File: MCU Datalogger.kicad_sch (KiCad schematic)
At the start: 25 parts, among them U1 24LC1025, U2 DS1337S_, U3 24LC1025, U4 ATMEGA328P-AU, Y1 32.768 KHz, Y2 16 MHz

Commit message: Completed Schematics and worked on comments
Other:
- note added: "ATMEGA MCU"
- note added: "EEPROM"
- note added: "Mounting Holes"
- note added: "Real Time Clock"
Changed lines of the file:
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@@
+		)
+	)
+	(rectangle
+		(start 29.21 129.54)
+		(end 133.35 175.26)
+		(stroke
+			(width 0)
+			(type default)
+		)
+		(fill
+			(type none)
+		)
+	)
+	(rectangle
+		(start 224.79 120.65)
+		(end 251.46 154.94)
+		(stroke
+			(width 0)
+			(type default)
+		)
+		(fill
+			(type none)
+		)
+	)
+	(rectangle
+		(start 140.97 22.86)
+		(end 266.7 110.49)
+		(stroke
+			(width 0)
+			(type default)
+		)
+		(fill
+			(type none)
+		)
+	)
+	(rectangle
+		(start 36.83 38.1)
+		(end 130.81 86.36)
+		(stroke
+			(width 0)
+			(type default)
+		)
+		(fill
+			(type none)
+		)
+	)
+	(text "Mounting Holes"
+		(exclude_from_sim no)
+		(at 232.41 119.38 0)
+		(effects
+			(font
+				(size 1.27 1.27)
+			)
+		)
+	)
+	(text "EEPROM"
+		(exclude_from_sim no)
+		(at 33.02 128.27 0)
+		(effects
+			(font
+				(size 1.27 1.27)
+			)
+		)
+	)
+	(text "ATMEGA MCU"
+		(exclude_from_sim no)
+		(at 147.32 20.32 0)
+		(effects
+			(font
+				(size 1.27 1.27)
+			)
+		)
+	)
+	(text "Real Time Clock"
+		(exclude_from_sim no)
+		(at 44.45 36.83 0)
+		(effects
+			(font
+				(size 1.27 1.27)
+			)
 		)
 	)

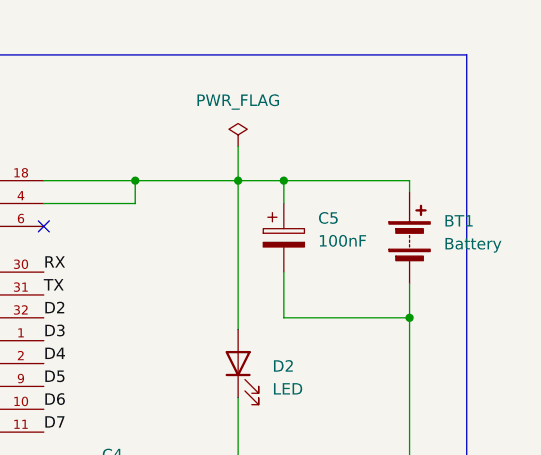
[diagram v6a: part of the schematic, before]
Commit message: Finished routing, silkscreen setup of the 2layer pcb
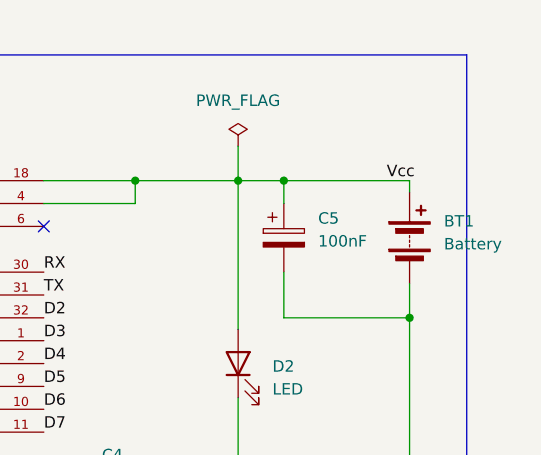
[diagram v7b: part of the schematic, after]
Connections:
- net Vcc: now also BT1.1 (+), C5.1, D2.2 (A), U4.18 (AVCC), U4.4 (VCC)
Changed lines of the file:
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@@
+		)
+	)
+	(label "Vcc"
+		(at 257.81 36.83 0)
+		(fields_autoplaced yes)
+		(effects
+			(font
+				(size 1.27 1.27)
+			)
+			(justify left bottom)
 		)
 	)

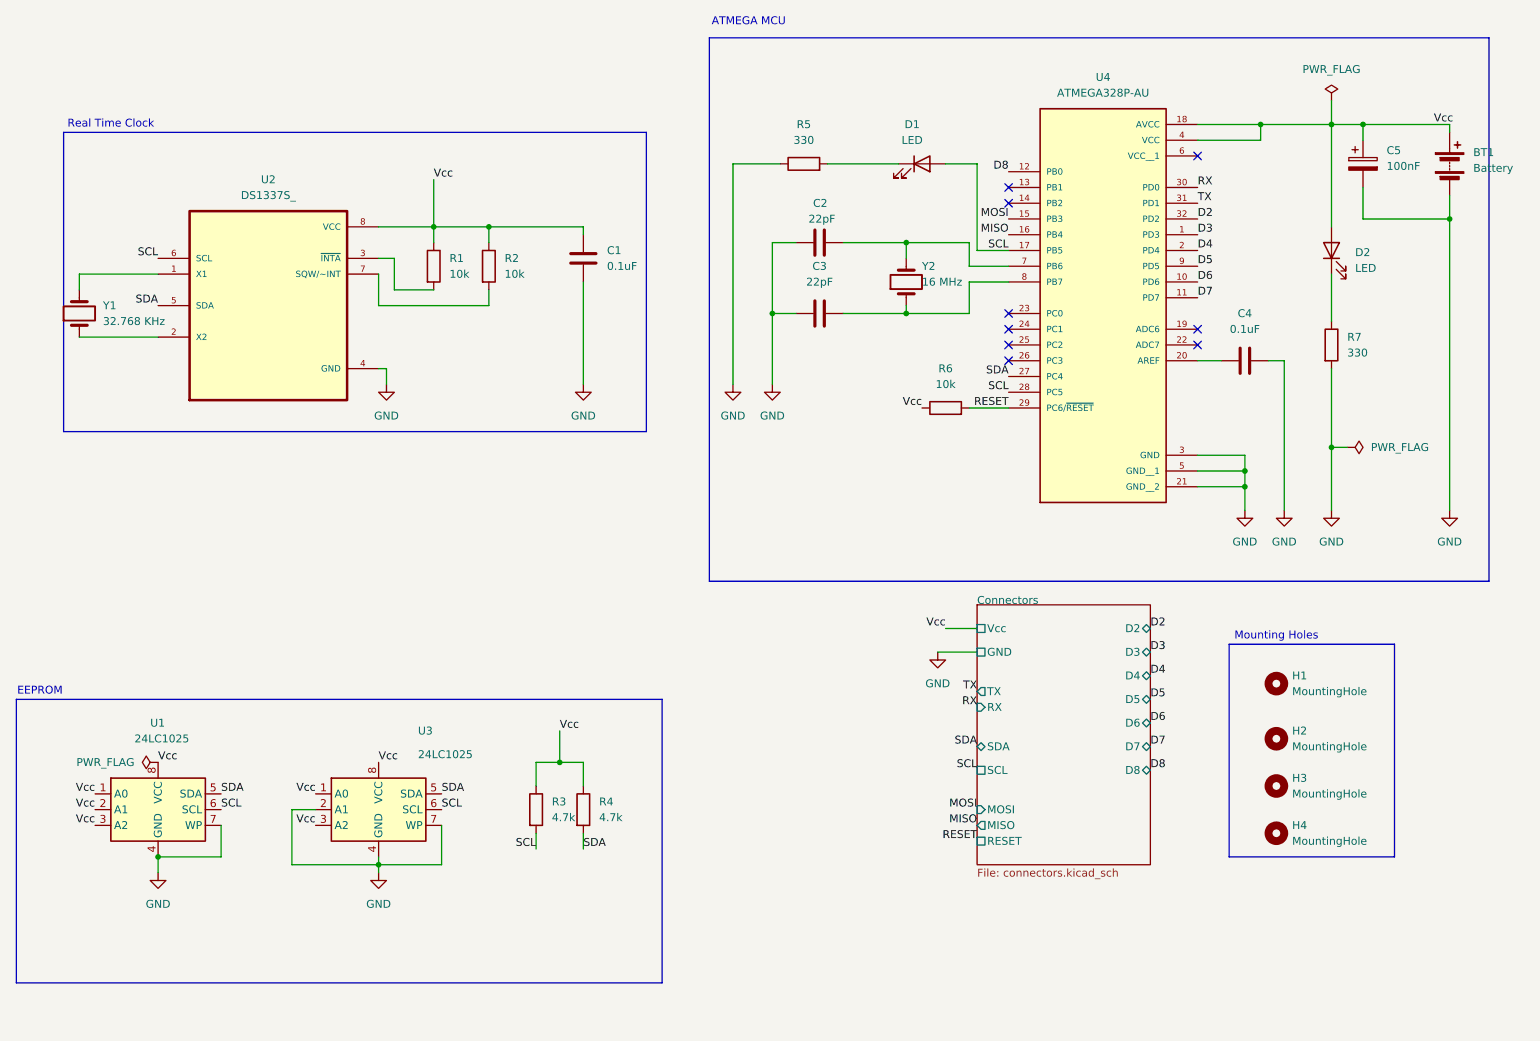
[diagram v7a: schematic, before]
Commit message: Fixed errors in the schematic
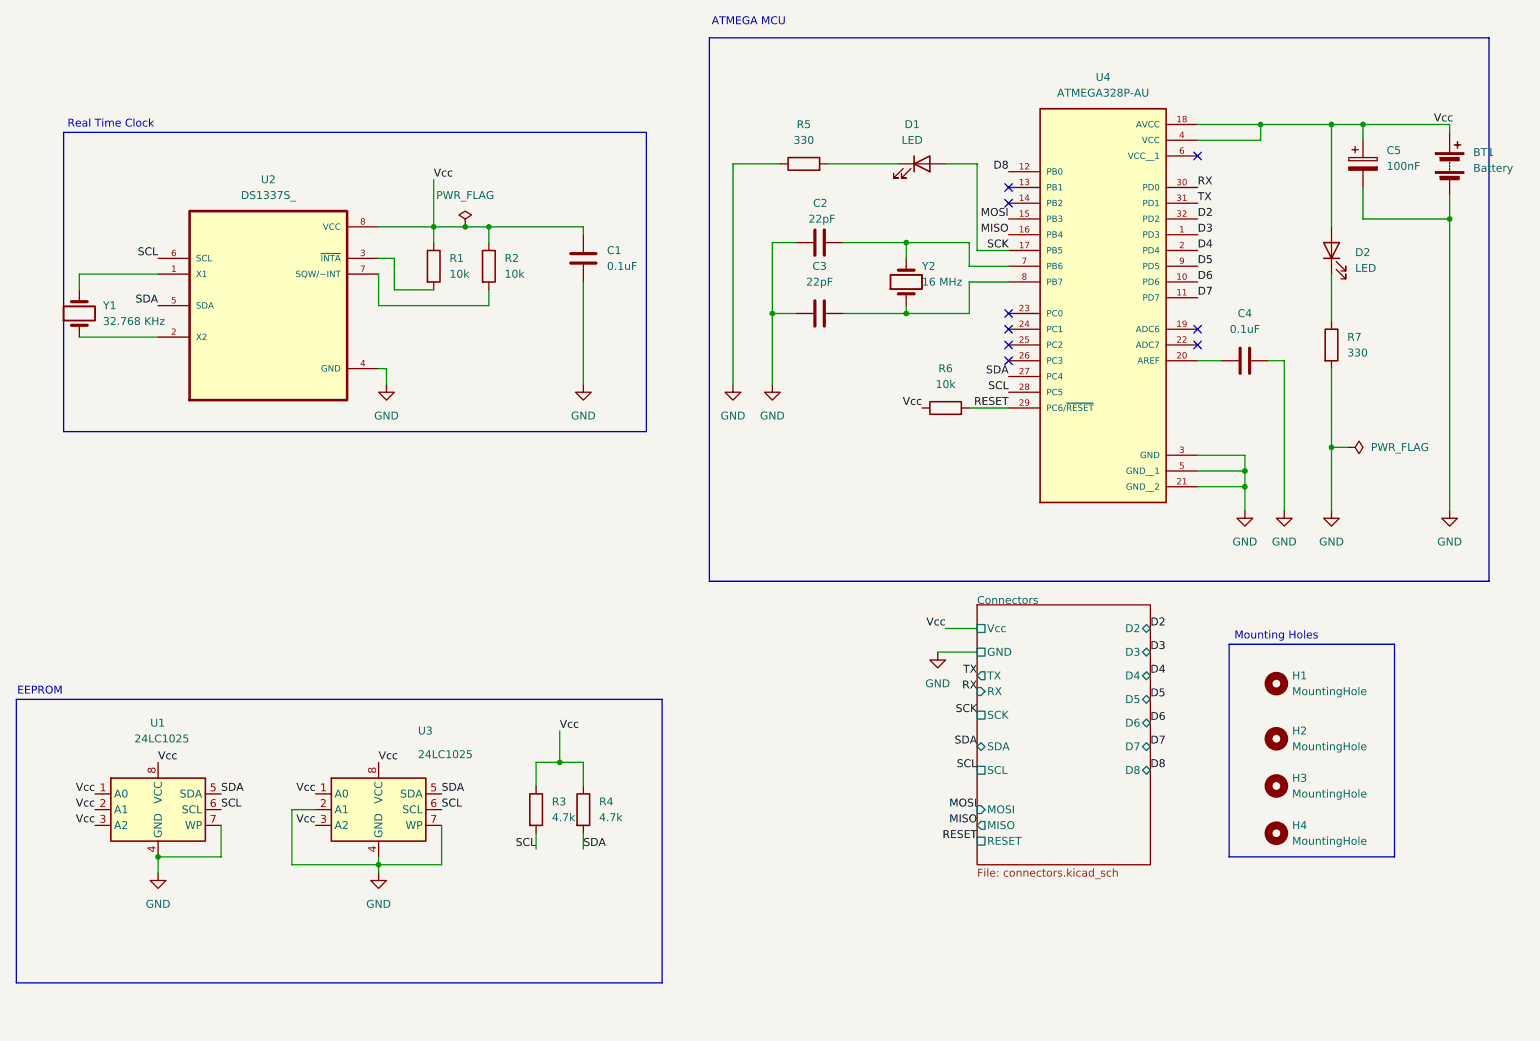
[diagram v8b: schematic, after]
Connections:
- net SCL: no longer D1.2 (A), U4.17 (PB5)
- new net SCK: D1.2 (A), U4.17 (PB5)
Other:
- sheet Connectors ports: added SCK; removed none
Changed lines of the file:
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@@
 	)
 	(junction
+		(at 101.6 53.34)
+		(diameter 0)
+		(color 0 0 0 0)
+	)
+	(junction
 		(at 229.87 36.83)
 		(diameter 0)
@@
 	(wire
 		(pts
-			(xy 241.3 33.02) (xy 241.3 36.83)
-		)
-		(stroke
-			(width 0)
-			(type default)
-		)
-	)
-	(wire
-		(pts
 			(xy 62.23 154.94) (xy 52.07 154.94)
 		)
@@
 	(wire
 		(pts
+			(xy 101.6 53.34) (xy 105.41 53.34)
+		)
+		(stroke
+			(width 0)
+			(type default)
+		)
+	)
+	(wire
+		(pts
 			(xy 77.47 147.32) (xy 73.66 147.32)
 		)
@@
 	(wire
 		(pts
+			(xy 105.41 53.34) (xy 120.65 53.34)
+		)
+		(stroke
+			(width 0)
+			(type default)
+		)
+	)
+	(wire
+		(pts
 			(xy 241.3 76.2) (xy 241.3 88.9)
 		)
@@
 	(wire
 		(pts
-			(xy 96.52 53.34) (xy 105.41 53.34)
+			(xy 96.52 53.34) (xy 101.6 53.34)
 		)
 		(stroke
@@
 	(wire
 		(pts
-			(xy 105.41 53.34) (xy 120.65 53.34)
-		)
-		(stroke
-			(width 0)
-			(type default)
-		)
-	)
-	(wire
-		(pts
 			(xy 229.87 39.37) (xy 229.87 36.83)
 		)
@@
 		)
 	)
-	(label "SCL"
+	(label "SCK"
 		(at 189.23 57.15 180)
 		(fields_autoplaced yes)
@@
 		)
 	)
+	(label "SCK"
+		(at 184.15 132.08 180)
+		(fields_autoplaced yes)
+		(effects
+			(font
+				(size 1.27 1.27)
+			)
+			(justify right bottom)
+		)
+	)
 	(label "TX"
 		(at 219.71 49.53 0)
@@
 	)
 	(label "RX"
-		(at 184.15 130.81 180)
+		(at 184.15 128.27 180)
 		(fields_autoplaced yes)
 		(effects
@@
 	)
 	(label "TX"
-		(at 184.15 128.27 180)
+		(at 184.15 125.73 180)
 		(fields_autoplaced yes)
 		(effects
@@
 	)
 	(symbol
-		(lib_id "power:PWR_FLAG")
-		(at 52.07 139.7 90)
-		(unit 1)
-		(exclude_from_sim no)
-		(in_bom yes)
-		(on_board yes)
-		(dnp no)
-		(fields_autoplaced yes)
-		(property "Reference" "#FLG03"
-			(at 50.165 139.7 0)
-			(effects
-				(font
-					(size 1.27 1.27)
-				)
-				(hide yes)
-			)
-		)
-		(property "Value" "PWR_FLAG"
-			(at 48.26 139.6999 90)
-			(effects
-				(font
-					(size 1.27 1.27)
-				)
-				(justify left)
-			)
-		)
-		(property "Footprint" ""
-			(at 52.07 139.7 0)
-			(effects
-				(font
-					(size 1.27 1.27)
-				)
-				(hide yes)
-			)
-		)
-		(property "Datasheet" "~"
-			(at 52.07 139.7 0)
-			(effects
-				(font
-					(size 1.27 1.27)
-				)
-				(hide yes)
-			)
-		)
-		(property "Description" "Special symbol for telling ERC where power comes from"
-			(at 52.07 139.7 0)
-			(effects
-				(font
-					(size 1.27 1.27)
-				)
-				(hide yes)
-			)
-		)
-		(pin "1"
-		)
-		(instances
-			(project "MCU Datalogger"
-				(path "/f5eacbf3-5133-41a8-b529-b36a541e7d42"
-					(reference "#FLG03")
-					(unit 1)
-				)
-			)
-		)
-	)
-	(symbol
 		(lib_id "Mechanical:MountingHole")
 		(at 232.41 151.13 0)
@@
 	)
 	(symbol
-		(lib_id "power:PWR_FLAG")
-		(at 241.3 33.02 0)
-		(unit 1)
-		(exclude_from_sim no)
-		(in_bom yes)
-		(on_board yes)
-		(dnp no)
-		(fields_autoplaced yes)
-		(property "Reference" "#FLG01"
-			(at 241.3 31.115 0)
-			(effects
-				(font
-					(size 1.27 1.27)
-				)
-				(hide yes)
-			)
-		)
-		(property "Value" "PWR_FLAG"
-			(at 241.3 27.94 0)
-			(effects
-				(font
-					(size 1.27 1.27)
-				)
-			)
-		)
-		(property "Footprint" ""
-			(at 241.3 33.02 0)
-			(effects
-				(font
-					(size 1.27 1.27)
-				)
-				(hide yes)
-			)
-		)
-		(property "Datasheet" "~"
-			(at 241.3 33.02 0)
-			(effects
-				(font
-					(size 1.27 1.27)
-				)
-				(hide yes)
-			)
-		)
-		(property "Description" "Special symbol for telling ERC where power comes from"
-			(at 241.3 33.02 0)
-			(effects
-				(font
-					(size 1.27 1.27)
-				)
-				(hide yes)
-			)
-		)
-		(pin "1"
-		)
-		(instances
-			(project "MCU Datalogger"
-				(path "/f5eacbf3-5133-41a8-b529-b36a541e7d42"
-					(reference "#FLG01")
-					(unit 1)
-				)
-			)
-		)
-	)
-	(symbol
 		(lib_id "Device:R")
 		(at 179.07 82.55 90)
@@
 		)
 	)
+	(symbol
+		(lib_id "power:PWR_FLAG")
+		(at 101.6 53.34 0)
+		(unit 1)
+		(exclude_from_sim no)
+		(in_bom yes)
+		(on_board yes)
+		(dnp no)
+		(fields_autoplaced yes)
+		(property "Reference" "#FLG04"
+			(at 101.6 51.435 0)
+			(effects
+				(font
+					(size 1.27 1.27)
+				)
+				(hide yes)
+			)
+		)
+		(property "Value" "PWR_FLAG"
+			(at 101.6 48.26 0)
+			(effects
+				(font
+					(size 1.27 1.27)
+				)
+			)
+		)
+		(property "Footprint" ""
+			(at 101.6 53.34 0)
+			(effects
+				(font
+					(size 1.27 1.27)
+				)
+				(hide yes)
+			)
+		)
+		(property "Datasheet" "~"
+			(at 101.6 53.34 0)
+			(effects
+				(font
+					(size 1.27 1.27)
+				)
+				(hide yes)
+			)
+		)
+		(property "Description" "Special symbol for telling ERC where power comes from"
+			(at 101.6 53.34 0)
+			(effects
+				(font
+					(size 1.27 1.27)
+				)
+				(hide yes)
+			)
+		)
+		(pin "1"
+		)
+		(instances
+			(project "MCU Datalogger"
+				(path "/f5eacbf3-5133-41a8-b529-b36a541e7d42"
+					(reference "#FLG04")
+					(unit 1)
+				)
+			)
+		)
+	)
 	(sheet
 		(at 184.15 114.3)
@@
 		)
 		(pin "RX" input
-			(at 184.15 130.81 180)
+			(at 184.15 128.27 180)
 			(effects
 				(font
@@
 		)
 		(pin "TX" output
-			(at 184.15 128.27 180)
+			(at 184.15 125.73 180)
 			(effects
 				(font
@@
 			(effects
 				(font
+					(size 1.27 1.27)
+				)
+				(justify left)
+			)
+		)
+		(pin "SCK" passive
+			(at 184.15 132.08 180)
+			(effects
+				(font
